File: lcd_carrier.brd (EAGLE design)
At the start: 80 x 36.2 mm, 23 parts, among them IC1 MCP2300X/SO, IC2 74LS595D, U1 LCD-16X2SILK

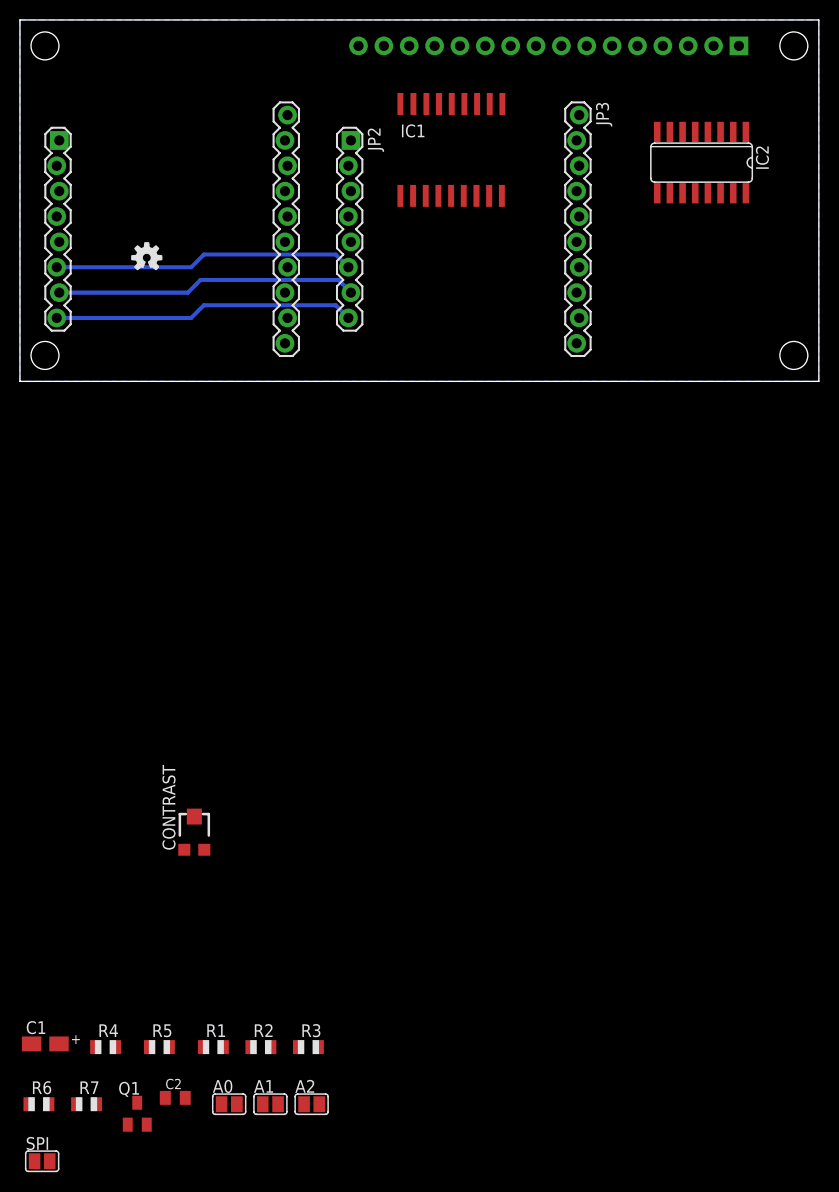
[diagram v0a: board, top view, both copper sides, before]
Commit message: Adding LCD carrier board
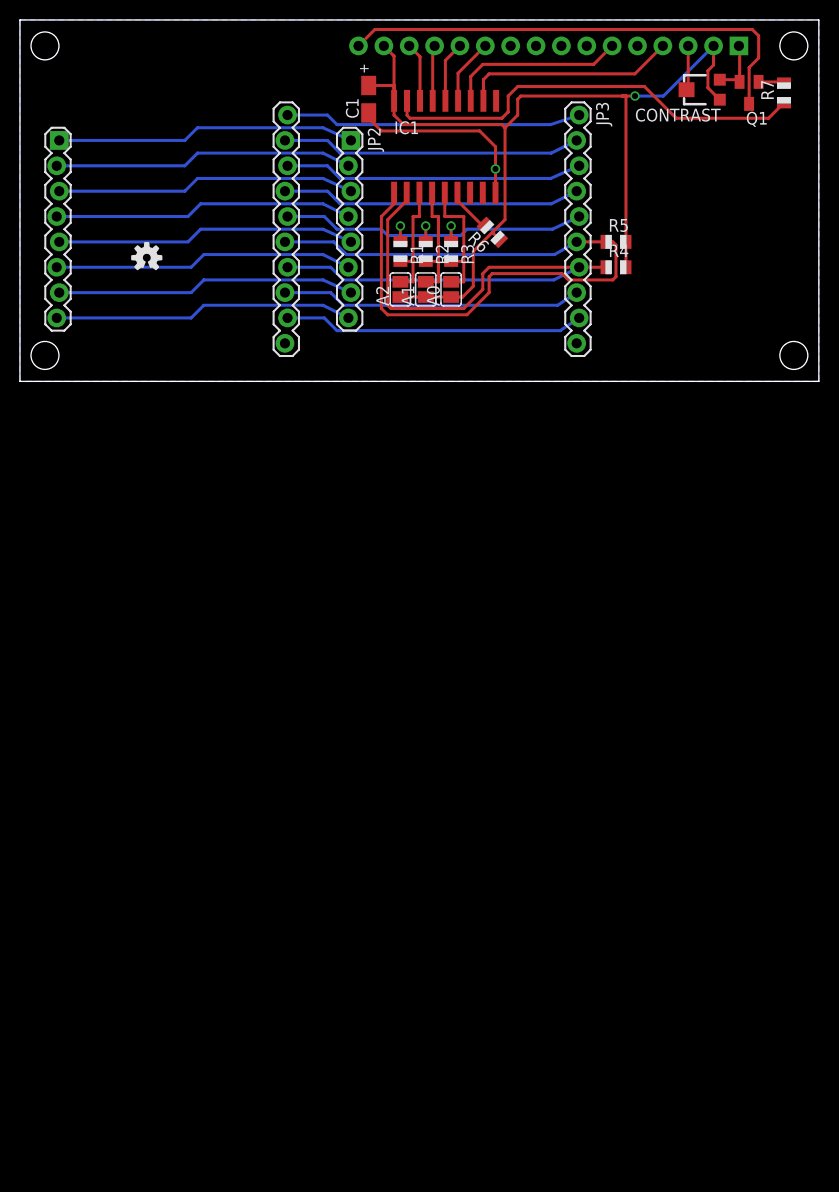
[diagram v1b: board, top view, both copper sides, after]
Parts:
- removed C2: 0.1uF, adafruit:C0805K
- removed IC2: 74LS595D, 74xx-us:SO16
- removed SPI: (no value), jumper:SJ
- moved R7 123.0 mm to (76.5, 28.9), turned to 90 degrees
- moved Q1 119.2 mm to (73.0, 28.9), turned to 180 degrees
- moved C1 100.0 mm to (34.9, 28.3), turned to 90 degrees
- moved R6 98.4 mm to (47.3, 14.9), turned to 135 degrees
- moved R4 93.3 mm to (59.7, 11.4)
- moved R5 92.7 mm to (59.7, 14.0)
- moved CONTRAST 90.0 mm to (68.3, 29.2), turned to 90 degrees
- moved A0 84.6 mm to (43.2, 9.21), turned to 90 degrees
- moved A1 83.1 mm to (40.6, 9.21), turned to 90 degrees
- moved A2 82.1 mm to (38.1, 9.21), turned to 90 degrees
- moved R1 81.9 mm to (38.1, 13.0), turned to 270 degrees
- moved R2 81.4 mm to (40.6, 13.0), turned to 270 degrees
- moved R3 81.0 mm to (43.2, 13.0), turned to 270 degrees
- moved IC1 0.71 mm to (41.9, 23.5)
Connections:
- removed net N$8: IC1.6, IC2.13, R6.2, SPI.2
- new net N$2: IC1.6, R6.2
- net DB4: no longer IC2.6
- net DB5: no longer IC2.5
- net DB6: no longer IC2.4
- net DB7: no longer IC2.3
- net E: no longer IC2.2
- net GND: no longer C2.2, IC2.8, SPI.1
- net LITE: no longer IC2.7
- net RS: no longer IC2.1
- net SCK/I2C_SCL: no longer IC2.11
- net SDI/I2C_SDA: no longer IC2.14
- net SDO: no longer IC2.12
- net VCC: no longer C2.1, IC2.10, IC2.16
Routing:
- net VCC: track 0.00 -> 97.8 mm, vias 0 -> 1
- net SCK/I2C_SCL: track 0.00 -> 76.2 mm
- net SDI/I2C_SDA: track 0.00 -> 66.7 mm
- net N$9: track 0.00 -> 48.2 mm
- net LITE: track 0.00 -> 43.5 mm
- net GND: track 0.00 -> 32.5 mm, vias 0 -> 4
- net SDO: track 0.00 -> 30.5 mm
- net RX: track 0.00 -> 30.1 mm
- net TX: track 0.00 -> 30.1 mm
- net RST: track 0.00 -> 30.0 mm
- net PGD: track 0.00 -> 30.0 mm
- net D3: track 0.00 -> 30.0 mm
- net D1: track 0.00 -> 30.0 mm
- net D4: track 0.00 -> 30.0 mm
- net D2: track 0.00 -> 30.0 mm
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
